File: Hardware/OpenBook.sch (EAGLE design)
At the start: 103 parts, among them IC1 XC6220A331MR-G, IC2 BD5229G-TR, J1 SAMACSYS_PARTS_USB4110-GF-A, J2 112A-TAAR-R03_ATTEND, J3 FH34SRJ-24S-0.5SH_99_, J4 QWIIC_RIGHT_ANGLE, Q1 20V/4.2A/52mΩ/1.4W, Q2 SI1308EDL-T1-GE3, Q3 20V/4.2A/52mΩ/1.4W, U1 BME688, U2 MCP73831, U3 ESP32-C6-WROOM-1-N8, U4 MAX17048G+T10, U5 DS3231SN#, U6 W25Q512JVEIQ

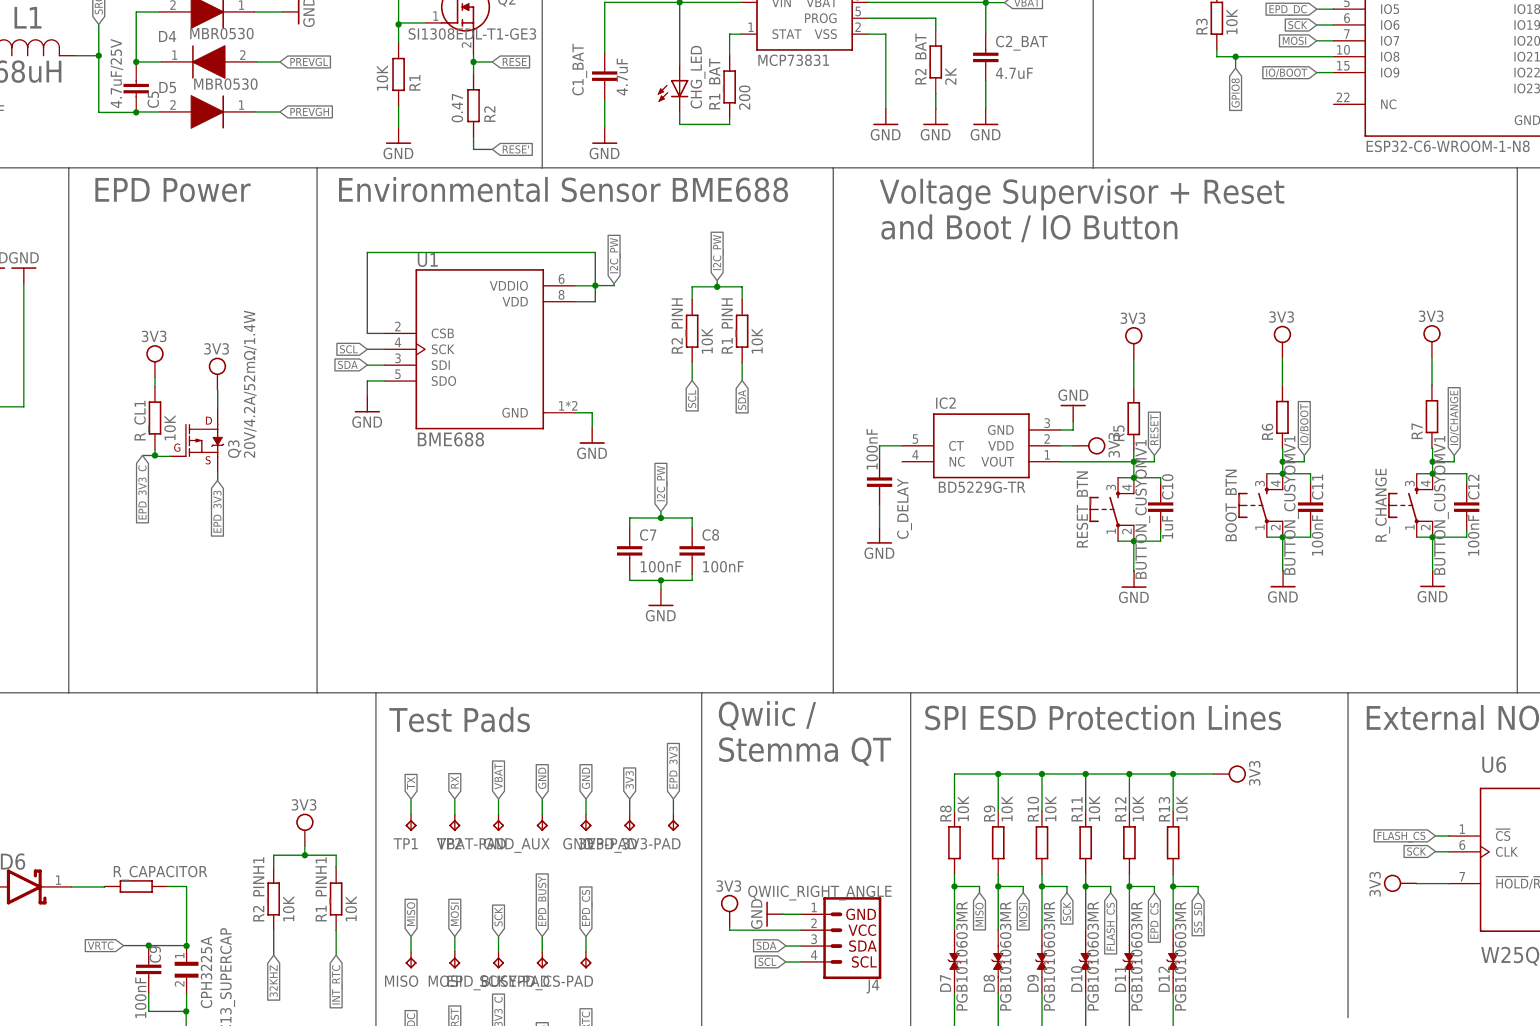
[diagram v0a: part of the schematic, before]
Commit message: Fixed some stuff
+Added via stitching around mcu
+Fixed inductor footprint with pads
+Added missing values to resistors
+Approved redundent erc warnings
+Fixed unconnected nets
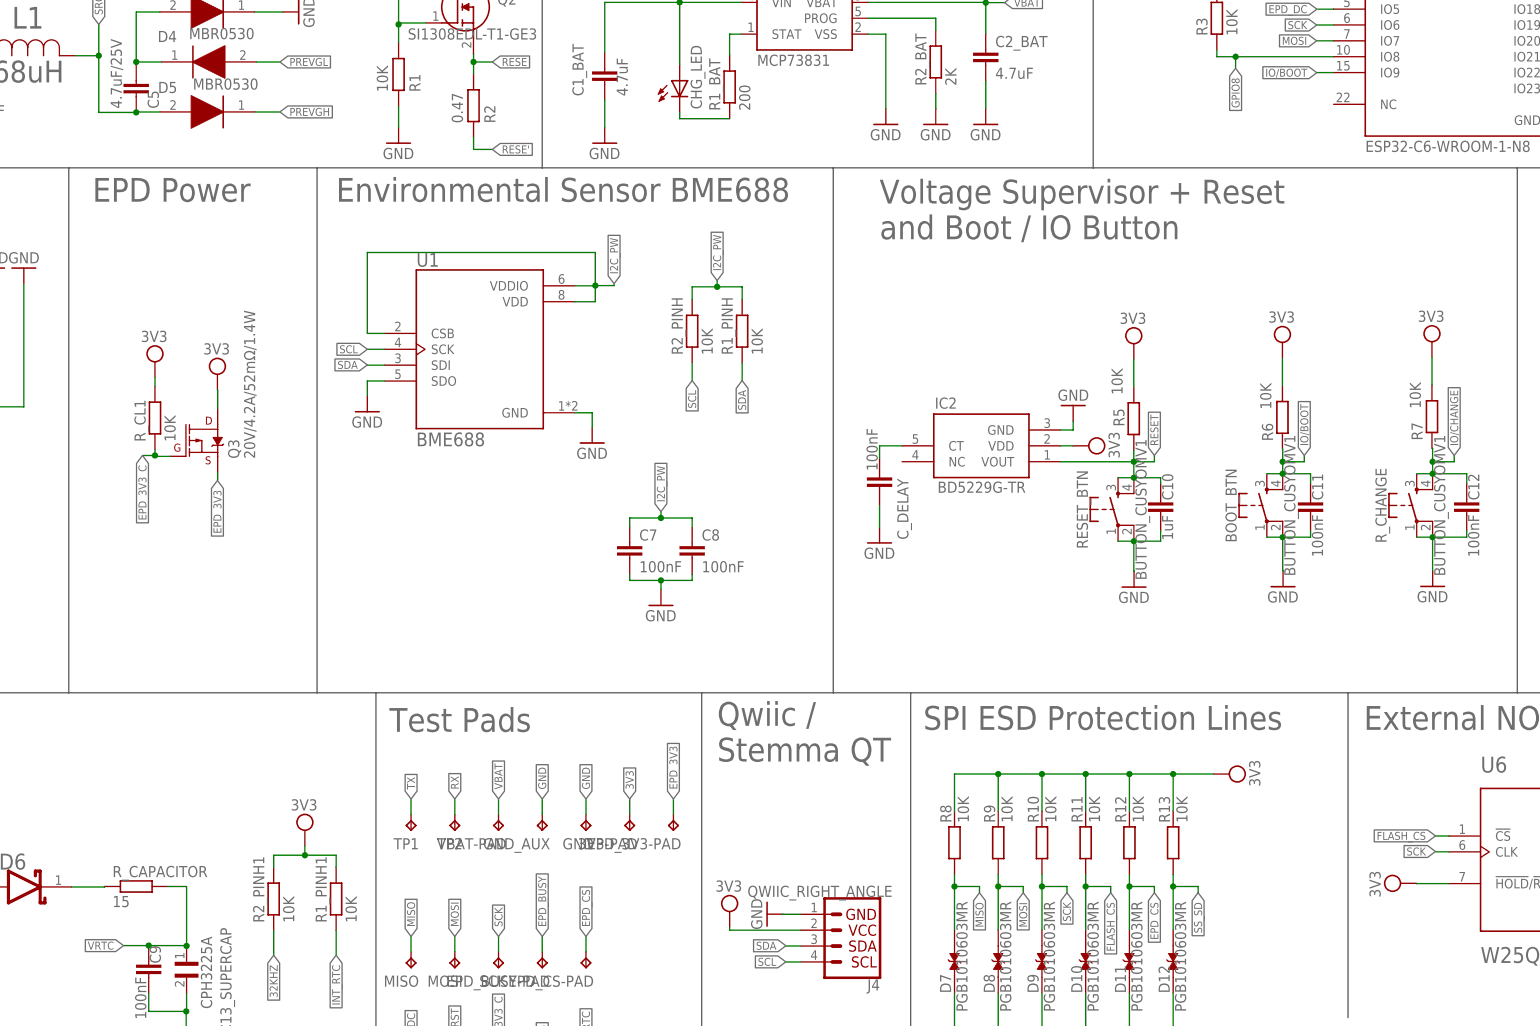
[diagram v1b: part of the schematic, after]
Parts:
- R5, R6, R7: value (none) -> 10K
- R_CAPACITOR: value (none) -> 15
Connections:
- net N$12: now also U2.STAT; no longer CHG_LED.C
- net N$14: now also CHG_LED.C; no longer U2.STAT
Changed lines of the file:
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@@
 <part name="SUPPLY8" library="DeskAssistant v19 v1" library_urn="urn:adsk.wipprod:fs.file:vf.2Vea2uG0TPukncocaLmiUQ" deviceset="3V3-CIRCLE" device="" value="3V3"/>
 <part name="SUPPLY9" library="DeskAssistant v19 v1" library_urn="urn:adsk.wipprod:fs.file:vf.2Vea2uG0TPukncocaLmiUQ" deviceset="3V3-CIRCLE" device="" value="3V3"/>
-<part name="R5" library="DeskAssistant v19 v1" library_urn="urn:adsk.wipprod:fs.file:vf.2Vea2uG0TPukncocaLmiUQ" deviceset="ESP32_WROVER_EAGLE-LTSPICE_R" device="R0402" package3d_urn="urn:adsk.eagle:package:47664233/1"/>
-<part name="R6" library="DeskAssistant v19 v1" library_urn="urn:adsk.wipprod:fs.file:vf.2Vea2uG0TPukncocaLmiUQ" deviceset="ESP32_WROVER_EAGLE-LTSPICE_R" device="R0402" package3d_urn="urn:adsk.eagle:package:47664233/1"/>
-<part name="R7" library="DeskAssistant v19 v1" library_urn="urn:adsk.wipprod:fs.file:vf.2Vea2uG0TPukncocaLmiUQ" deviceset="ESP32_WROVER_EAGLE-LTSPICE_R" device="R0402" package3d_urn="urn:adsk.eagle:package:47664233/1"/>
+<part name="R5" library="DeskAssistant v19 v1" library_urn="urn:adsk.wipprod:fs.file:vf.2Vea2uG0TPukncocaLmiUQ" deviceset="ESP32_WROVER_EAGLE-LTSPICE_R" device="R0402" package3d_urn="urn:adsk.eagle:package:47664233/1" value="10K"/>
+<part name="R6" library="DeskAssistant v19 v1" library_urn="urn:adsk.wipprod:fs.file:vf.2Vea2uG0TPukncocaLmiUQ" deviceset="ESP32_WROVER_EAGLE-LTSPICE_R" device="R0402" package3d_urn="urn:adsk.eagle:package:47664233/1" value="10K"/>
+<part name="R7" library="DeskAssistant v19 v1" library_urn="urn:adsk.wipprod:fs.file:vf.2Vea2uG0TPukncocaLmiUQ" deviceset="ESP32_WROVER_EAGLE-LTSPICE_R" device="R0402" package3d_urn="urn:adsk.eagle:package:47664233/1" value="10K"/>
 <part uuid="2882400021" name="RESET_BTN" library="DeskAssistant v19 v1" library_urn="urn:adsk.wipprod:fs.file:vf.2Vea2uG0TPukncocaLmiUQ" deviceset="BUTTON_CUSYOMV1" device="" package3d_urn="urn:adsk.eagle:package:47664215/1"/>
 <part name="BOOT_BTN" library="DeskAssistant v19 v1" library_urn="urn:adsk.wipprod:fs.file:vf.2Vea2uG0TPukncocaLmiUQ" deviceset="BUTTON_CUSYOMV1" device="" package3d_urn="urn:adsk.eagle:package:47664215/1"/>
@@
 <part name="R2_PINH1" library="DeskAssistant v19 v1" library_urn="urn:adsk.wipprod:fs.file:vf.2Vea2uG0TPukncocaLmiUQ" deviceset="ESP32_WROVER_EAGLE-LTSPICE_R" device="R0402" package3d_urn="urn:adsk.eagle:package:47664233/1" value="10K"/>
 <part name="R1_PINH1" library="DeskAssistant v19 v1" library_urn="urn:adsk.wipprod:fs.file:vf.2Vea2uG0TPukncocaLmiUQ" deviceset="ESP32_WROVER_EAGLE-LTSPICE_R" device="R0402" package3d_urn="urn:adsk.eagle:package:47664233/1" value="10K"/>
-<part name="R_CAPACITOR" library="DeskAssistant v19 v1" library_urn="urn:adsk.wipprod:fs.file:vf.2Vea2uG0TPukncocaLmiUQ" deviceset="ESP32_WROVER_EAGLE-LTSPICE_R" device="R0402" package3d_urn="urn:adsk.eagle:package:47664233/1"/>
+<part name="R_CAPACITOR" library="DeskAssistant v19 v1" library_urn="urn:adsk.wipprod:fs.file:vf.2Vea2uG0TPukncocaLmiUQ" deviceset="ESP32_WROVER_EAGLE-LTSPICE_R" device="R0402" package3d_urn="urn:adsk.eagle:package:47664233/1" value="15"/>
 <part name="D6" library="DeskAssistant v19 v1" library_urn="urn:adsk.wipprod:fs.file:vf.2Vea2uG0TPukncocaLmiUQ" deviceset="ESP32_WROVER_AVX---SD0805S020S1R0_AVX_SD0805S020S1R0_0_0" device="AVX_SD0805S020S1R0_0_0" package3d_urn="urn:adsk.eagle:package:47664231/1"/>
 <part name="GND39" library="DeskAssistant v19 v1" library_urn="urn:adsk.wipprod:fs.file:vf.2Vea2uG0TPukncocaLmiUQ" deviceset="GND" device=""/>
@@
 </instance>
 <instance part="R5" gate="G$1" x="289.7" y="142.9" smashed="yes" rot="R90">
-<attribute name="NAME" x="288.2014" y="139.09" size="1.778" layer="95" rot="R90"/>
-<attribute name="VALUE" x="293.002" y="139.09" size="1.778" layer="96" rot="R90"/>
-<attribute name="NAME" x="288.2014" y="139.09" size="1.778" layer="95" rot="R90"/>
-<attribute name="VALUE" x="293.002" y="139.09" size="1.778" layer="96" rot="R90"/>
+<attribute name="NAME" x="288.2014" y="141.63" size="1.778" layer="95" rot="R90"/>
+<attribute name="VALUE" x="287.922" y="146.71" size="1.778" layer="96" rot="R90"/>
 </instance>
 <instance part="R6" gate="G$1" x="313.5" y="143.1" smashed="yes" rot="R90">
 <attribute name="NAME" x="312.0014" y="139.29" size="1.778" layer="95" rot="R90"/>
-<attribute name="VALUE" x="316.802" y="139.29" size="1.778" layer="96" rot="R90"/>
 <attribute name="NAME" x="312.0014" y="139.29" size="1.778" layer="95" rot="R90"/>
-<attribute name="VALUE" x="316.802" y="139.29" size="1.778" layer="96" rot="R90"/>
+<attribute name="VALUE" x="311.722" y="144.37" size="1.778" layer="96" rot="R90"/>
 </instance>
 <instance part="R7" gate="G$1" x="337.44" y="143.22" smashed="yes" rot="R90">
 <attribute name="NAME" x="335.9414" y="139.41" size="1.778" layer="95" rot="R90"/>
-<attribute name="VALUE" x="340.742" y="139.41" size="1.778" layer="96" rot="R90"/>
 <attribute name="NAME" x="335.9414" y="139.41" size="1.778" layer="95" rot="R90"/>
-<attribute name="VALUE" x="340.742" y="139.41" size="1.778" layer="96" rot="R90"/>
+<attribute name="VALUE" x="335.662" y="144.49" size="1.778" layer="96" rot="R90"/>
 </instance>
 <instance part="RESET_BTN" gate="G$1" x="287.18" y="128.36" smashed="yes" rot="R90">
@@
 <junction x="124" y="201"/>
 <label x="124" y="206" size="1.27" layer="95" rot="R90" xref="yes"/>
-<pinref part="L1" gate="A" pin="1"/>
 <pinref part="C5" gate="G$1" pin="2"/>
 <pinref part="D5" gate="G$1" pin="A"/>
+<pinref part="L1" gate="A" pin="1"/>
 </segment>
 <segment>
@@
 <junction x="103" y="201"/>
 <label x="103" y="206" size="1.27" layer="95" rot="R90" xref="yes"/>
+<pinref part="C6" gate="G$1" pin="1"/>
 <pinref part="L1" gate="A" pin="2"/>
-<pinref part="C6" gate="G$1" pin="1"/>
 </segment>
 <segment>
@@
 </segment>
 </net>
-<net name="N$12" class="0">
-<segment>
-<wire x1="217" y1="191.92" x2="217" y2="190" width="0.1524" layer="91"/>
-<wire x1="217" y1="190" x2="225" y2="190" width="0.1524" layer="91"/>
-<wire x1="225" y1="190" x2="225" y2="190.92" width="0.1524" layer="91"/>
-<pinref part="R1_BAT" gate="G$1" pin="2"/>
+<net name="N$14" class="0">
+<segment>
+<pinref part="R1_BAT" gate="G$1" pin="1"/>
+<wire x1="225" y1="190.92" x2="217" y2="190.92" width="0.1524" layer="91"/>
+<wire x1="217" y1="190.92" x2="217" y2="191.92" width="0.1524" layer="91"/>
 <pinref part="CHG_LED" gate="G$1" pin="C"/>
-</segment>
-</net>
-<net name="N$14" class="0">
-<segment>
-<wire x1="225" y1="201.08" x2="225" y2="204.46" width="0.1524" layer="91"/>
-<wire x1="225" y1="204.46" x2="226.84" y2="204.46" width="0.1524" layer="91"/>
-<pinref part="R1_BAT" gate="G$1" pin="1"/>
-<pinref part="U2" gate="G$1" pin="STAT"/>
 </segment>
 </net>
@@
 </segment>
 </net>
+<net name="N$12" class="0">
+<segment>
+<pinref part="R1_BAT" gate="G$1" pin="2"/>
+<wire x1="225" y1="201.08" x2="225" y2="204.46" width="0.1524" layer="91"/>
+<wire x1="225" y1="204.46" x2="226.84" y2="204.46" width="0.1524" layer="91"/>
+<pinref part="U2" gate="G$1" pin="STAT"/>
+</segment>
+</net>
 </nets>
 </sheet>
 </sheets>
+<errors>
+</errors>
 </schematic>
 </drawing>
